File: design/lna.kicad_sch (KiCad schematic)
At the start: 22 parts, among them J5 SMA, U9 ADA4930-1

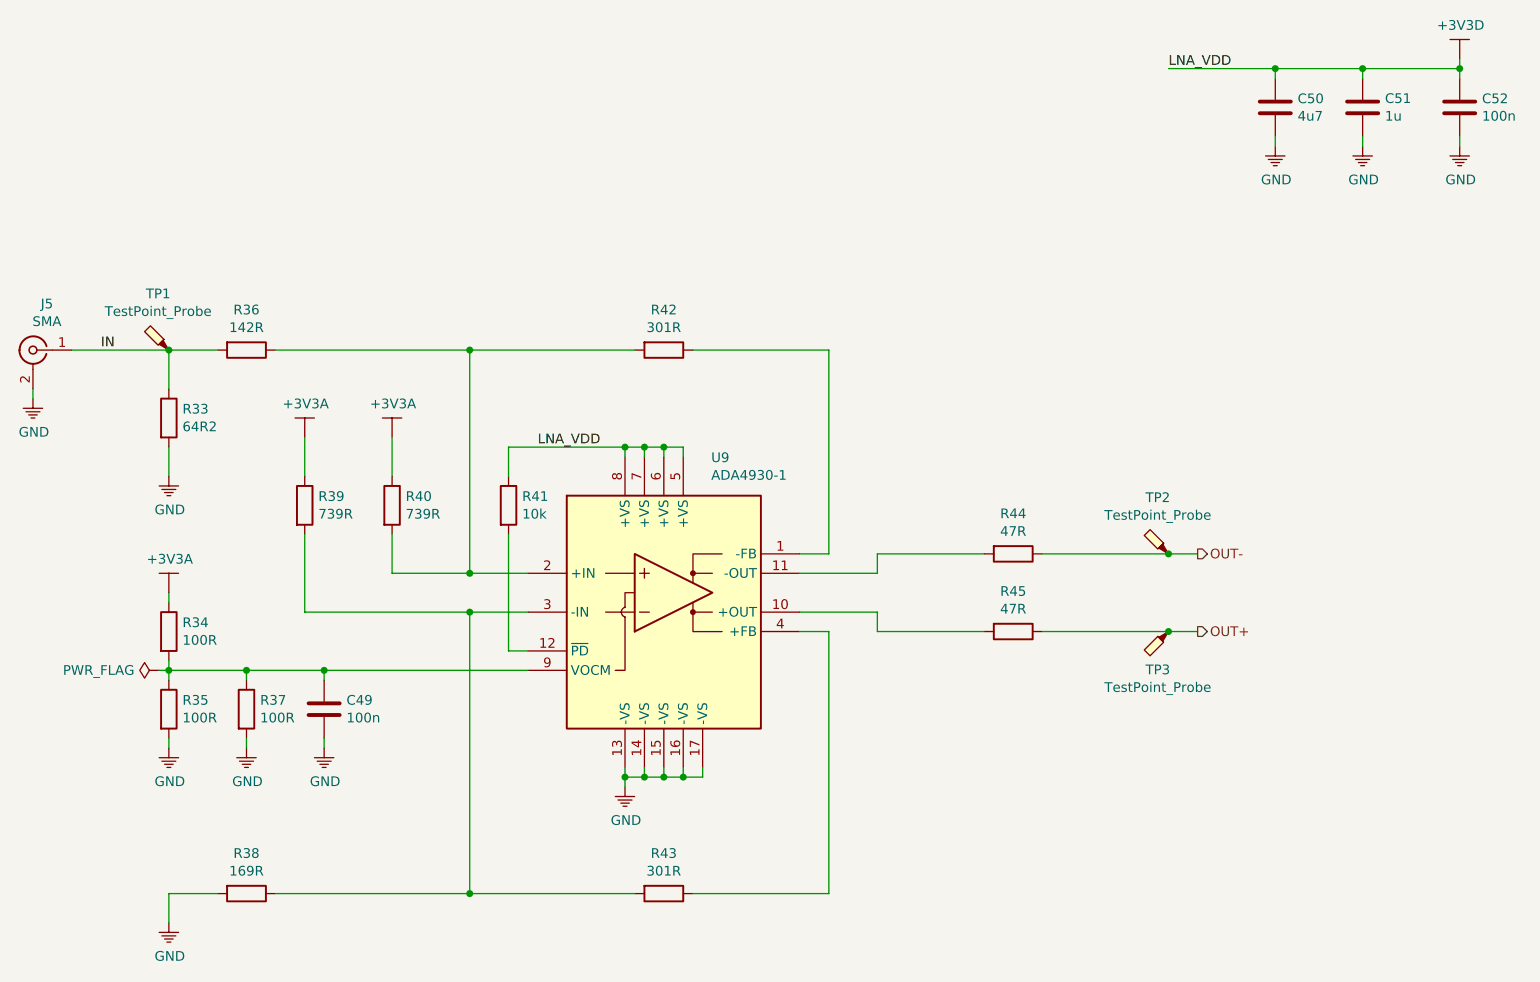
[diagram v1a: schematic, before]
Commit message: Fixed LNA power
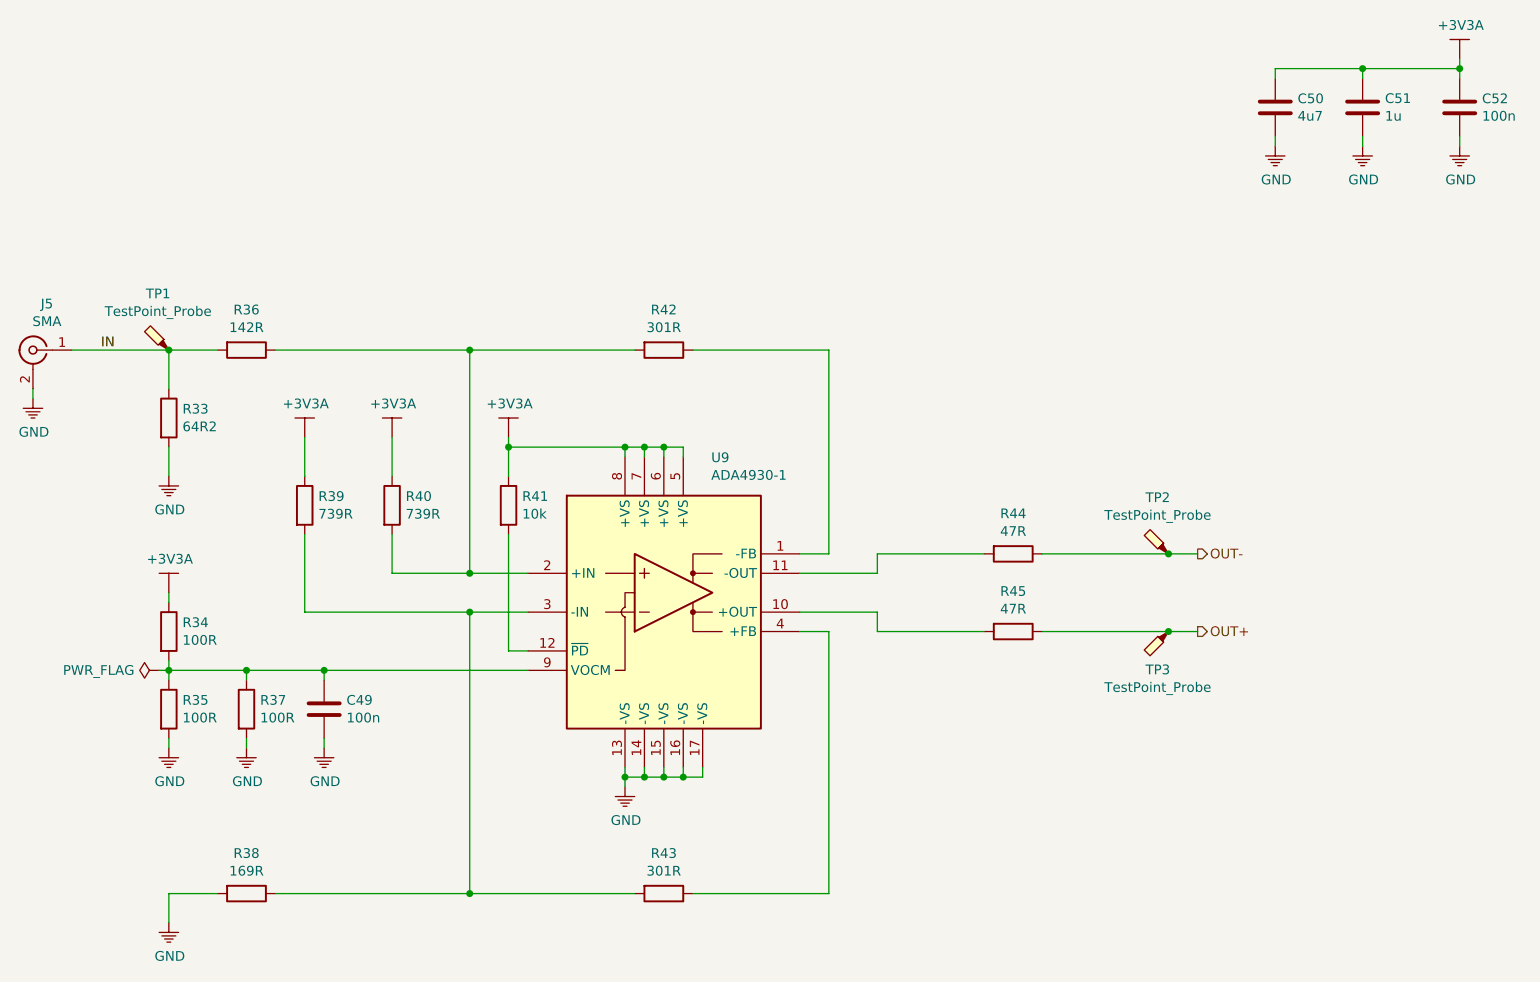
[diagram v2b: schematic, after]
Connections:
- net +3V3D is gone; now on net +3V3A: C50.1, C51.1, C52.1, R41.1, U9.5 (+VS), U9.6 (+VS), U9.7 (+VS), U9.8 (+VS)
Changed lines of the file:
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@@
-(kicad_sch (version 20200310) (host eeschema "5.99.0-unknown-5cf474e~101~ubuntu18.04.1")
+(kicad_sch (version 20200506) (host eeschema "5.99.0-unknown-1f9723c~101~ubuntu18.04.1")
   (page "A4")
   (title_block
@@
     (comment 2 "figure 50")
   )
+  (junction (at 144.78 119.38))
+  (junction (at 147.32 76.2))
+  (junction (at 129.54 76.2))
+  (junction (at 124.46 63.5))
+  (junction (at 144.78 76.2))
+  (junction (at 95.25 105.41))
   (junction (at 152.4 119.38))
+  (junction (at 241.3 26.67))
+  (junction (at 85.09 105.41))
   (junction (at 124.46 97.79))
-  (junction (at 144.78 76.2))
+  (junction (at 124.46 92.71))
+  (junction (at 147.32 119.38))
+  (junction (at 149.86 119.38))
+  (junction (at 149.86 76.2))
   (junction (at 215.9 90.17))
-  (junction (at 241.3 26.67))
-  (junction (at 144.78 119.38))
-  (junction (at 149.86 76.2))
-  (junction (at 149.86 119.38))
-  (junction (at 147.32 76.2))
-  (junction (at 95.25 105.41))
-  (junction (at 85.09 105.41))
-  (junction (at 124.46 63.5))
-  (junction (at 147.32 119.38))
+  (junction (at 215.9 100.33))
+  (junction (at 254 26.67))
+  (junction (at 85.09 63.5))
   (junction (at 105.41 105.41))
-  (junction (at 124.46 92.71))
-  (junction (at 85.09 63.5))
   (junction (at 124.46 134.62))
-  (junction (at 215.9 100.33))
-  (junction (at 229.87 26.67))
-  (junction (at 254 26.67))
   (wire (pts (xy 67.31 69.85) (xy 67.31 68.58)))
   (wire (pts (xy 83.82 105.41) (xy 85.09 105.41)))
@@
   (wire (pts (xy 124.46 97.79) (xy 132.08 97.79)))
   (wire (pts (xy 124.46 134.62) (xy 146.05 134.62)))
+  (wire (pts (xy 129.54 74.93) (xy 129.54 76.2)))
   (wire (pts (xy 129.54 76.2) (xy 144.78 76.2)))
   (wire (pts (xy 129.54 80.01) (xy 129.54 76.2)))
@@
   (wire (pts (xy 199.39 90.17) (xy 215.9 90.17)))
   (wire (pts (xy 199.39 100.33) (xy 215.9 100.33)))
-  (wire (pts (xy 215.9 26.67) (xy 229.87 26.67)))
   (wire (pts (xy 215.9 90.17) (xy 219.71 90.17)))
   (wire (pts (xy 219.71 100.33) (xy 215.9 100.33)))
@@
     (effects (font (size 1.27 1.27)) (justify left bottom))
   )
-  (label "LNA_VDD" (at 133.35 76.2 0)
-    (effects (font (size 1.27 1.27)) (justify left bottom))
-  )
-  (label "LNA_VDD" (at 215.9 26.67 0)
-    (effects (font (size 1.27 1.27)) (justify left bottom))
-  )
   (hierarchical_label "OUT-" (shape output) (at 219.71 90.17 0)
     (effects (font (size 1.27 1.27)) (justify left))
@@
     )
   )
+  (symbol (lib_id "KLIB_Power:+3V3A") (at 129.54 74.93 0) (unit 1)
+    (property "Reference" "#PWR0139" (id 0) (at 129.54 82.55 0)
+      (effects (font (size 1.27 1.27)) hide)
+    )
+    (property "Value" "+3V3A" (id 1) (at 129.667 70.5358 0))
+    (property "Footprint" "" (id 2) (at 129.54 74.93 0)
+      (effects (font (size 1.27 1.27)) hide)
+    )
+    (property "Datasheet" "" (id 3) (at 129.54 74.93 0)
+      (effects (font (size 1.27 1.27)) hide)
+    )
+  )
   (symbol (lib_id "KLIB_Power:GND") (at 144.78 120.65 0) (unit 1)
     (property "Reference" "#PWR0106" (id 0) (at 144.78 125.73 0)
@@
     )
   )
-  (symbol (lib_id "KLIB_Power:+3V3D") (at 254 25.4 0) (unit 1)
-    (property "Reference" "#PWR0109" (id 0) (at 254 33.02 0)
-      (effects (font (size 1.27 1.27)) hide)
-    )
-    (property "Value" "+3V3D" (id 1) (at 254.127 21.0058 0))
+  (symbol (lib_id "KLIB_Power:+3V3A") (at 254 25.4 0) (unit 1)
+    (property "Reference" "#PWR0139" (id 0) (at 254 33.02 0)
+      (effects (font (size 1.27 1.27)) hide)
+    )
+    (property "Value" "+3V3A" (id 1) (at 254.127 21.0058 0))
     (property "Footprint" "" (id 2) (at 254 25.4 0)
       (effects (font (size 1.27 1.27)) hide)
